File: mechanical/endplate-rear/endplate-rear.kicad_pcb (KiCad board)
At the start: 2 copper layers, 88 x 38 mm, 0 parts

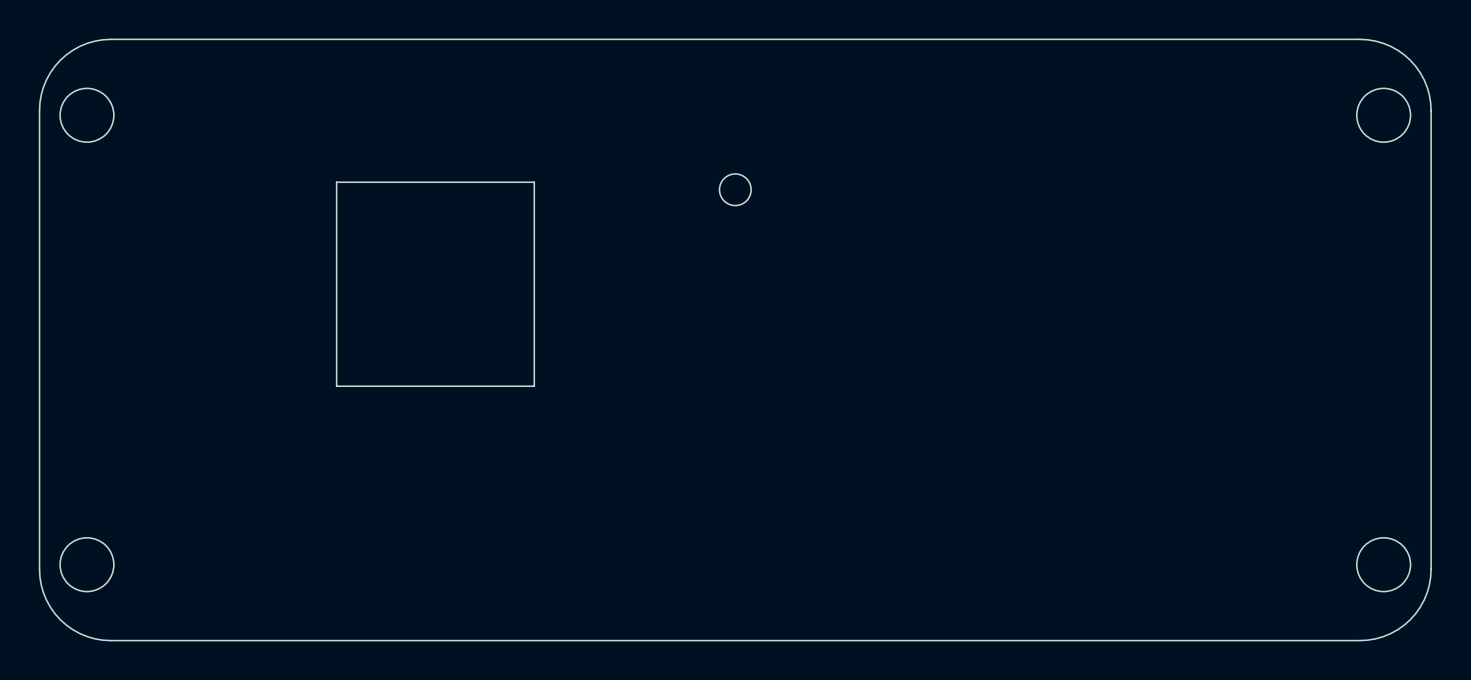
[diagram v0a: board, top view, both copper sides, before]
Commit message: end-plate GND shield, DRC, and fab notes (#69)
* throwaway: exercise design -> dev pipeline (safe to delete)

* Bring over ringof/dev (tranche 2, stage 1): design, library, 3D, board CI & docs

* Bring over ringof/dev (tranche 2, stage 2): mechanical enclosure + 3D viewer

* run_checks: hard-fail the 3D-model check regardless of ENFORCE

* Improved 3D viewer (#59)

* mechanical: give the end plates a Blue soldermask stackup

The end-plate PCBs had no physical stackup, so KiCad exported them with the
default green soldermask. Add a 2-layer stackup with front/back mask set to the
named "Blue" preset, summing to the existing 1.6 mm so board thickness / fit is
unchanged. This makes the plates export blue-dominant so the viewer's soldermask
recolour treats them the same as the main board.

* feat(viewer): part toggles, upright orientation, Turn Island navy, even lighting

Grow the mechanical fit-check viewer into an interactive, correctly-coloured one:

- Part toggles: show/hide enclosure, main board, front/rear end plate. Rebuilt on
  pinned three.js r148 (model-viewer has no per-node visibility API); a checkbox
  flips object.visible on each part's prefixed nodes. Libraries inlined via a
  runtime import map -- no bundler, fully offline.
- Upright orientation (180 deg roll), click-to-set-pivot, and a header showing the
  git hash and branch as links (new --repo-url, fed from the CI environment).
- Board colour: assemble_glb recolours the blue soldermask to the Turn Island navy
  (KiCad's "Blue" preset exports a brighter cornflower); detection targets only the
  matte, blue-dominant mask material. The material is identical on every face, so
  the viewer lighting is set to an orientation-independent rig (soft key + strong
  ambient + damped environment) so every face reads the same navy.
- Checkbox reload-sync: autocomplete="off" + re-apply each box's state on load so
  the model always matches the checkboxes after a refresh.

Colour is applied downstream of KiCad (in th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
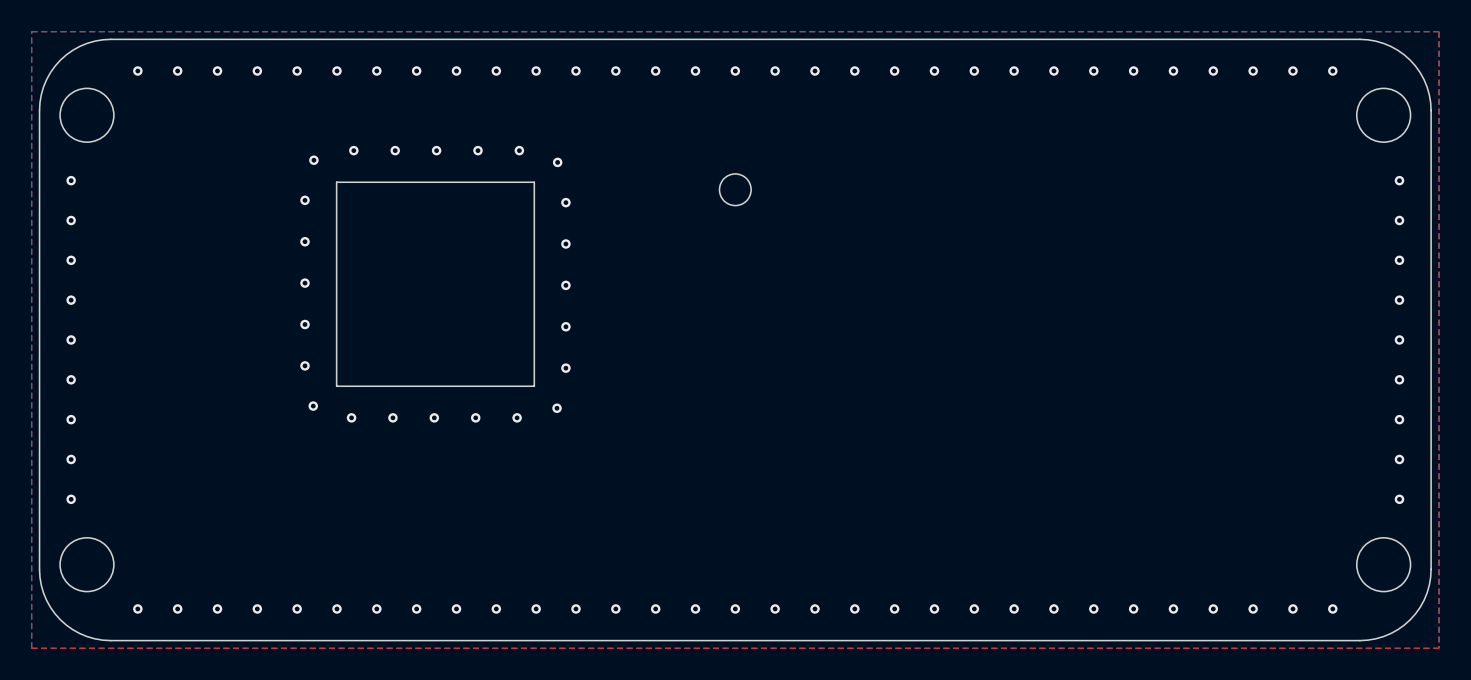
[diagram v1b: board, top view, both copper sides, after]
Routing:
- net GND: vias 0 -> 104
- added copper zone on B.Cu, net GND
- added copper zone on F.Cu, net GND
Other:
- board text added: "DESIGN NOTES ======================================== Outline 88x38mm R4.5mm; M3 corner holes Ø3.4mm USB 3.0 opening 12.5x12.9mm; STATUS hole Ø2.0mm to view the D3 LED (body-center aligned via fit-check). Shield: F+B copper pour, 0.3/0.6mm via stitch - perimeter ring + a ring around the USB opening. Ø7mm exposed-copper mask at each M3 (screw grounds shield to enclosure). Pour/via/mask/cutout-ring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"
- board text added: "FABRICATION SPECIFICATION ======================================== Project: TAPRX-888 Rear End Plate GENERAL Layers: 2 Material: FR4, standard Tg Finished Thickness: 1.6mm (~63 mil) +/-10% Surface Finish: ENIG Solder Mask: Blue, both sides Silkscreen: White, both sides IPC Class: 2 STACKUP F.Cu 1 oz (0.035mm) core 1.51mm FR4 (Er 4.5) B.Cu 1 oz (0.035mm) (1.6mm nominal, ENIG) CONTROLLED IMPEDANCE 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"
- board text removed: "REAR PLATE (USB). X-mirrored vs front (outside view). Non-functional enclosure end plate. Outline 88x38 R4.5; M3 corner holes Ø3.4 @ +/-41,+/-14.21 (plate screws on, full face). USB 3.0 opening 12.5x12.9 centered at plate (25.04, 15.49). STATUS hole Ø2.0 at plate (44.0, 9.0) to view the D3 LED (body-center aligned via the fit-check; D3 3D model +0.5 Z). plate Y from floor edge Y=0, +Y = up. Dimen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"
